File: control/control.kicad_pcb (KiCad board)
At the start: 2 copper layers, 100 x 40 mm, 54 parts, among them CON1 USB-MICRO-B, IC1 STM32F072CBT6, IC2 AD8495, IC3 ADP3335, P1 SWD, P2 CONN_02X04, P3 CONN_01X02, Q1 NPN, U1 ROTENC, U2 ESP8266, U3 ER-OLEDM023-1, U5 M3_HOLE, U6 M3_HOLE, U7 M3_HOLE, U8 M3_HOLE, X1 8MHz, X2 32k768

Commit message: first routing complete!
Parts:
- removed Q1: NPN, control:SOT23
- removed the R2 at (95.8, 127.8)
- added IC1: AD8542, control:MSOP8, B.Cu at (86.2, 136.5)
- added R1: 15k, control:R0603, B.Cu at (82.8, 135.5)
- added R3: 10k, control:R0603, B.Cu at (86.2, 129.5)
- added R5: 15k, control:R0603, B.Cu at (82.8, 133.5)
- added R6: 10k, control:R0603, B.Cu at (84.8, 129.5)
- moved SP1 13.2 mm to (98.5, 132.5), turned to 180 degrees
- moved BT1 12.4 mm to (110.5, 136.2), turned to 90 degrees
- moved C14 10.1 mm to (97.8, 113.2), turned to 0 degrees
- moved C15 9.40 mm to (97.8, 122.0), turned to 0 degrees
- moved C10 6.43 mm to (74.5, 107.8)
- moved C11 6.43 mm to (91.2, 109.5)
- moved C12 6.43 mm to (96.8, 109.5)
- moved C24 6.43 mm to (93.5, 122.2)
- moved C4 6.43 mm to (90.0, 111.2)
- moved C5 6.43 mm to (94.8, 121.0)
- moved C7 6.43 mm to (90.0, 112.5)
- moved C9 6.43 mm to (93.5, 121.0)
- moved IC2 6.43 mm to (91.0, 115.7)
- moved P1 6.43 mm to (81.0, 108.0)
- moved R7 6.43 mm to (96.0, 121.0)
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- renumbered C9 to C10, C12 to C11, C13 to C12, C19 to C13, C10 to C14, C11 to C15, C14 to C16, C15 to C17, C23 to C18, C24 to C19, C8 to C2, C25 to C20, C26 to C21, C16 to C22, C17 to C23, C18 to C24, C22 to C25, C2 to C3, C3 to C4, C4 to C5, C20 to C6, C5 to C7, C6 to C8, C7 to C9, IC1 to IC2, IC2 to IC4, R7 to R10, R9 to R11, R1 to R2, R3 to R4, R4 to R7, R5 to R8, R6 to R9, U3 to U4, X2 to X1, X1 to X2
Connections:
- IC2 pad 14: /PIEZO -> /PIEZO_A
- IC2 pad 15: /SYNC -> /PIEZO_B
- IC2 pad 18: /TRIAC -> /M_RELAY
- IC2 pad 20: /M_RELAY -> /TRIAC
- P2 pad 5: /SYNC -> Net-(P2-Pad5)
- P2 pad 7: VCC -> +5V
- P2 pad 8: +5V -> VCC
- SP1 pad 1: VCC -> Net-(IC1-Pad1)
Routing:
- net VDD: track 107.5 -> 283.8 mm, vias 0 -> 2
- net /ENC_BLU: track 0.00 -> 85.6 mm, vias 0 -> 4
- net /ENC_GRN: track 0.00 -> 81.8 mm, vias 0 -> 4
- net /ENC_SW: track 0.00 -> 81.4 mm, vias 0 -> 4
- net /ENC_B: track 3.42 -> 82.5 mm, vias 0 -> 4
- net /ENC_RED: track 0.00 -> 77.0 mm, vias 0 -> 4
- net /ENC_A: track 3.42 -> 75.7 mm, vias 0 -> 4
- net Net-(IC1-Pad2): track 0.00 -> 39.3 mm
- net /SYNC: track 30.0 -> 0.00 mm
- net Net-(BT1-Pad1): track 17.9 -> 42.8 mm
- net /nRST: track 1.55 -> 26.4 mm, vias 0 -> 5
- net VCC: track 51.3 -> 72.5 mm, vias 1 -> 0
- net Net-(IC1-Pad1): track 0.00 -> 19.1 mm
- net Net-(IC4-Pad5): track 69.4 -> 83.9 mm
- net /M_RELAY: track 30.2 -> 16.8 mm
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
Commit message: some routing improvements
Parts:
- added C26: 100n, control:C0603, B.Cu at (85.8, 129.5)
- moved R7 3.26 mm to (95.8, 117.8), turned to 180 degrees
- moved R3 0.75 mm to (87.0, 129.5)
- moved R6 0.25 mm to (84.5, 129.5)
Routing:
- net VDD: track 283.8 -> 292.8 mm
- net VCC: track 72.5 -> 75.7 mm
- net Net-(IC2-Pad6): track 5.91 -> 3.35 mm
- net Net-(C12-Pad2): track 10.7 -> 9.26 mm
- net Net-(C14-Pad1): track 11.0 -> 12.0 mm
- net Net-(C15-Pad1): track 5.65 -> 6.59 mm
- net Net-(IC1-Pad2): track 39.3 -> 38.6 mm
- net /PIEZO_A: track 7.32 -> 6.57 mm
- net GND: track 70.7 -> 71.1 mm, vias 18 -> 19

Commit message: update wifi, routing, gen gerbers, DONE r1
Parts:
- U2: value ESP8266 -> ESP8266-ESP01; footprint control:ESP8266 -> control:ESP8266-ESP01
- moved U2 19.1 mm to (55.7, 113.8), turned to 0 degrees
- moved C19 4.89 mm to (57.2, 130.1), turned to 180 degrees
- moved C8 1.25 mm to (81.5, 113.0)
- moved C3 1.20 mm to (81.5, 111.8)
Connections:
- CON1 pad 4: Net-(CON1-Pad4) -> (no net)
- CON1 pad 6: Net-(CON1-Pad6) -> (no net)
- CON1 pad 7: Net-(CON1-Pad7) -> (no net)
- IC2 pad 11: Net-(IC2-Pad11) -> (no net)
- IC2 pad 12: Net-(IC2-Pad12) -> (no net)
- IC2 pad 2: Net-(IC2-Pad2) -> (no net)
- IC2 pad 21: Net-(IC2-Pad21) -> (no net)
- IC2 pad 22: Net-(IC2-Pad22) -> /WIFI_RST
- IC2 pad 29: Net-(IC2-Pad29) -> /WIFI_GP0
- IC2 pad 40: Net-(IC2-Pad40) -> (no net)
- IC2 pad 45: Net-(IC2-Pad45) -> (no net)
- IC2 pad 46: Net-(IC2-Pad46) -> (no net)
- IC4 pad 4: Net-(IC4-Pad4) -> (no net)
- P1 pad 6: Net-(P1-Pad6) -> (no net)
- P1 pad 7: Net-(P1-Pad7) -> (no net)
- P1 pad 8: Net-(P1-Pad8) -> (no net)
- P2 pad 5: Net-(P2-Pad5) -> (no net)
- U2 pad 1: /WIFI_TX -> /WIFI_RX
- U2 pad 2: GND -> /WIFI_GP0
- U2 pad 3: Net-(U2-Pad3) -> (no net)
- U2 pad 4: Net-(U2-Pad4) -> GND
- U2 pad 5: Net-(U2-Pad5) -> /WIFI_TX
- U2 pad 6: Net-(U2-Pad6) -> VDD
- U2 pad 7: VDD -> /WIFI_RST
- U2 pad 8: /WIFI_RX -> VDD
- U4 pad 17: Net-(U4-Pad17) -> (no net)
- U4 pad 18: Net-(U4-Pad18) -> (no net)
- U4 pad 19: Net-(U4-Pad19) -> (no net)
- U4 pad 3: Net-(U4-Pad3) -> (no net)
- U4 pad 9: Net-(U4-Pad9) -> (no net)
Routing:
- net /WIFI_GP0: track 0.00 -> 18.9 mm, vias 0 -> 1
- net VDD: track 292.8 -> 307.3 mm
- net /WIFI_RST: track 0.00 -> 7.45 mm, vias 0 -> 1
- net VCC: track 75.7 -> 72.0 mm
- net /WIFI_RX: track 15.8 -> 13.6 mm
- net +5V: track 47.2 -> 45.1 mm
- net /WIFI_TX: track 5.82 -> 4.33 mm
- net /USB_DP: track 30.2 -> 30.9 mm
- net /USB_DM: track 30.1 -> 30.8 mm
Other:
- board text added: "ADAM GREIG DAVID TURNER JON SOWMAN"
- board text added: "GRN"
- board text added: "SUPERVIDE CONTROL BOARD"
- board text added: "r1 2014-03-06"
- board text added: "r1 2015-03-06"

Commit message: fix a few derps, actually DONE r1
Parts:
- moved C13 1.77 mm to (69.2, 105.0), turned to 180 degrees
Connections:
- U4 pad 1: VDD -> GND
- U4 pad 2: GND -> VDD
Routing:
- net VDD: track 307.3 -> 315.9 mm

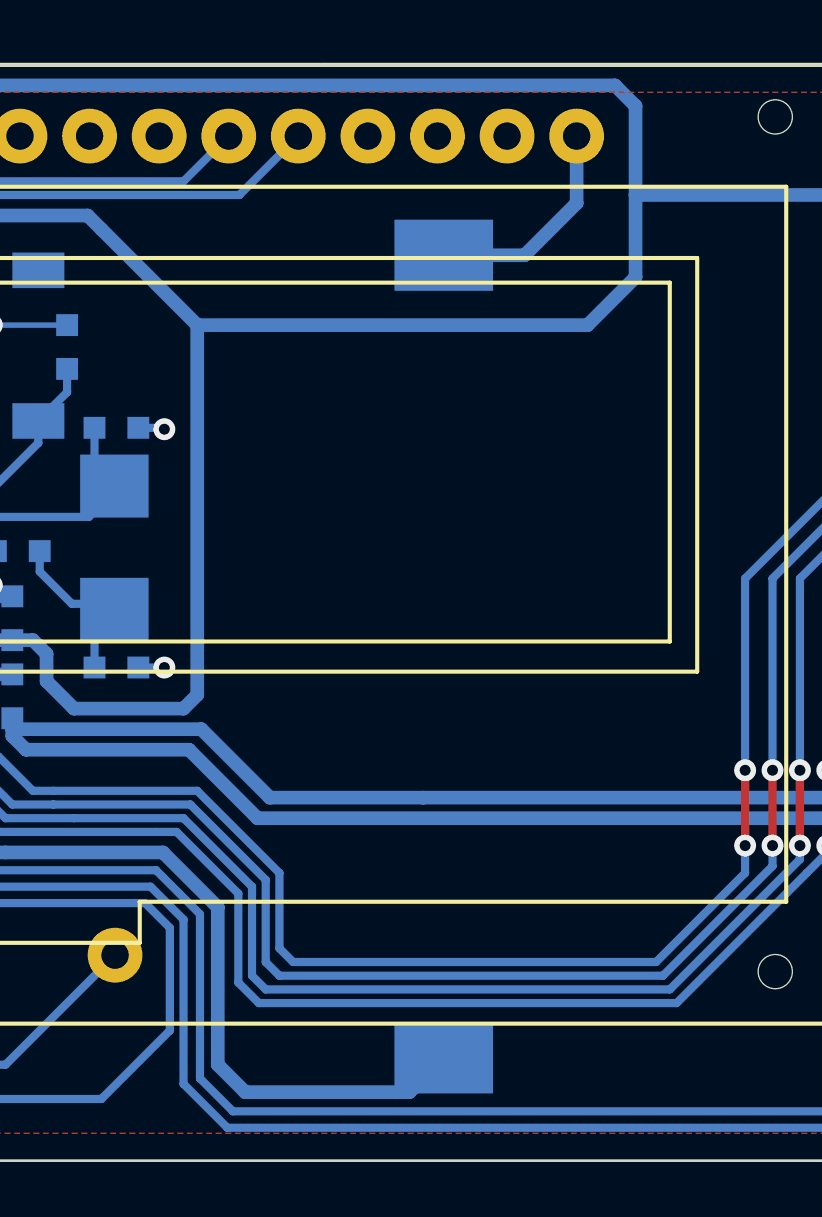
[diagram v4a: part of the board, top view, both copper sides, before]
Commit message: shift coin cell a little to make more space. still r1.
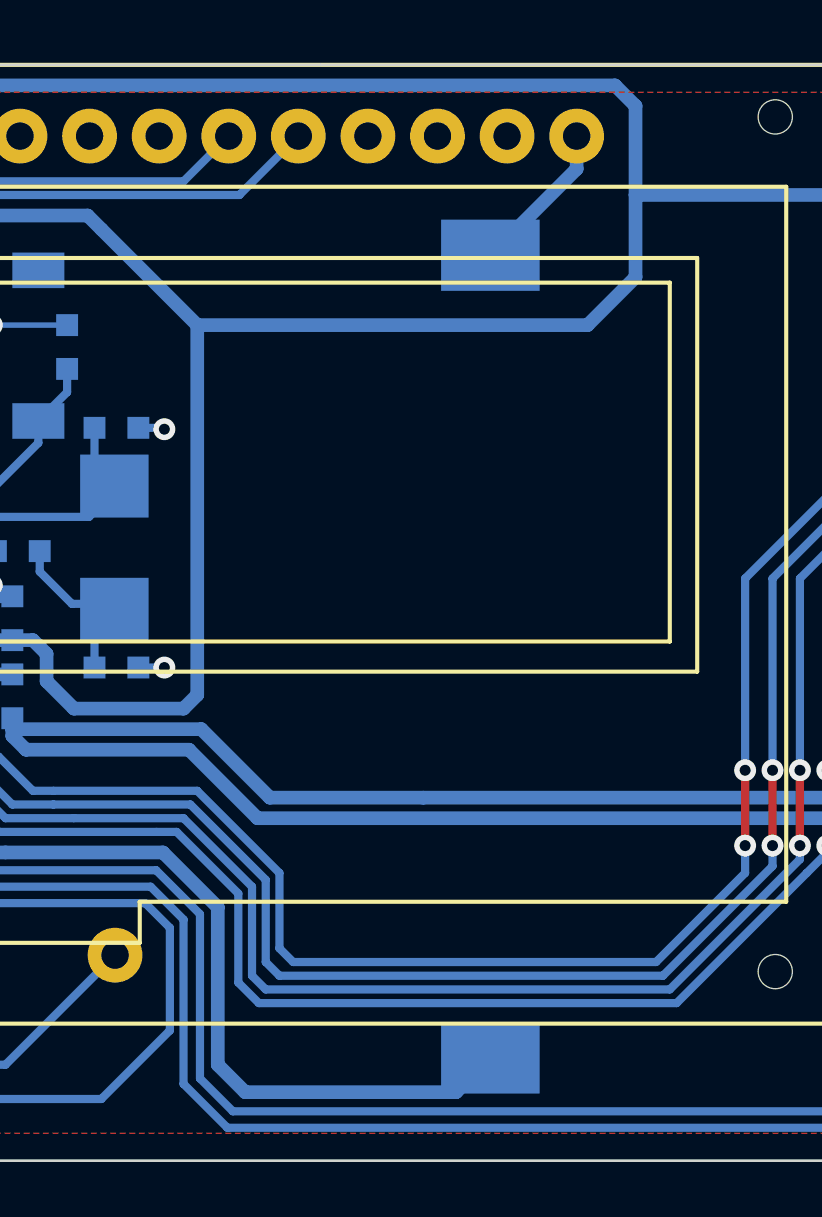
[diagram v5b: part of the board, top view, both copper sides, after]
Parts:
- moved BT1 1.70 mm to (112.2, 136.2)
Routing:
- net GND: track 71.1 -> 68.7 mm
- net Net-(BT1-Pad1): track 42.8 -> 44.5 mm

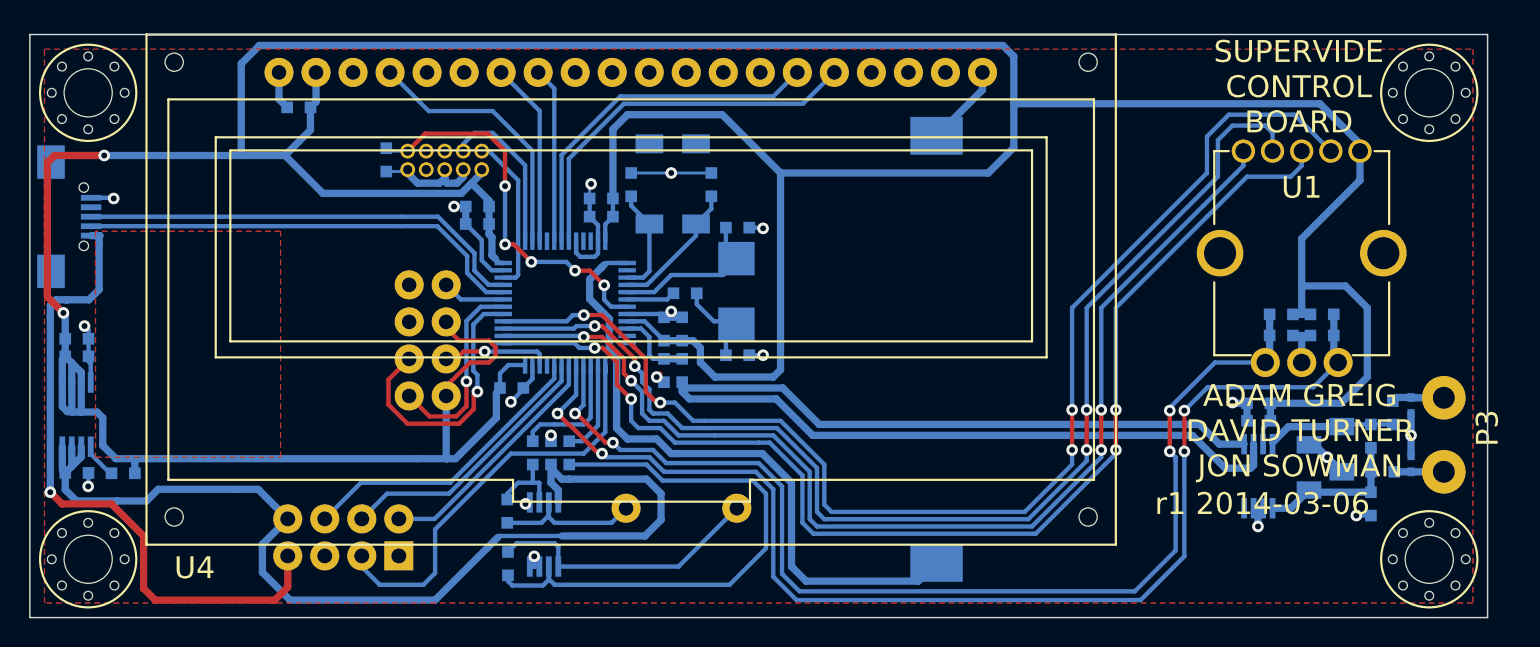
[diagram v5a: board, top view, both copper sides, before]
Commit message: regen gerbils w/ correct date on silk
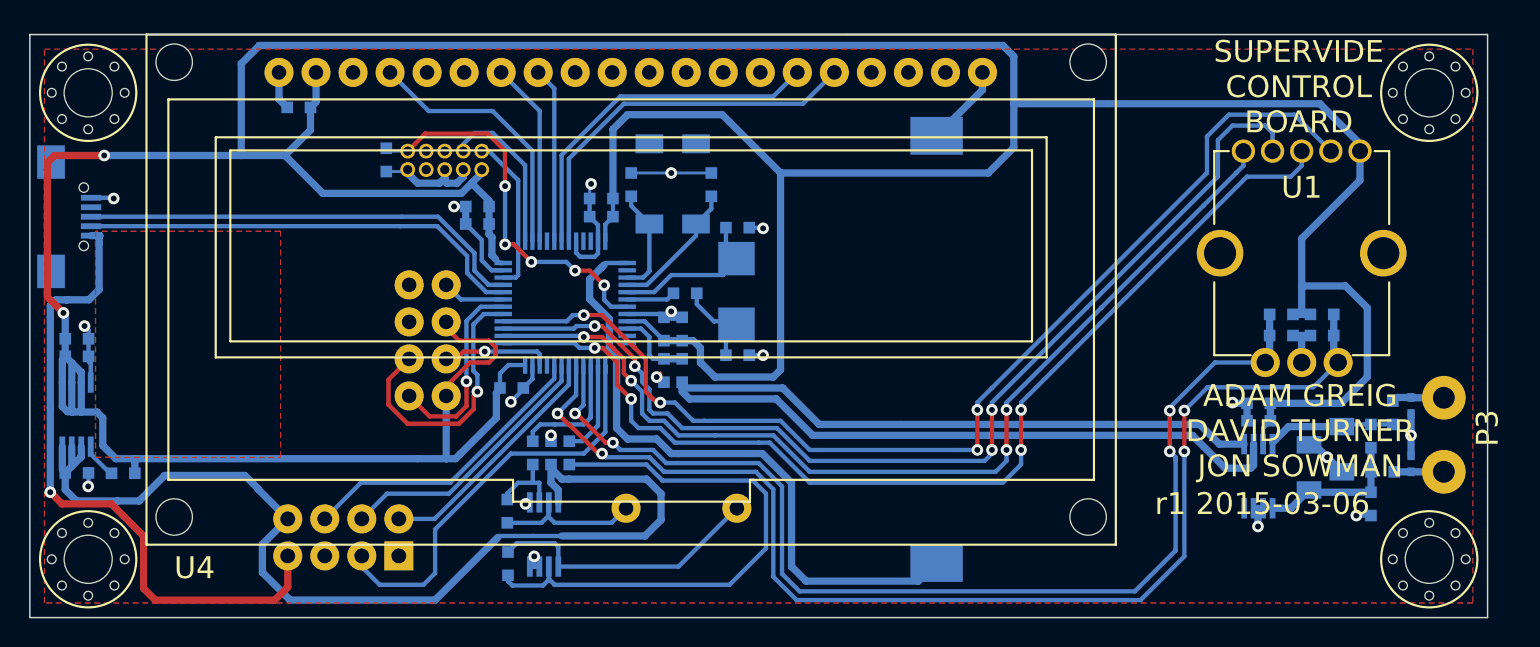
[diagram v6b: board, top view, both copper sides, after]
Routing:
- net /ENC_BLU: track 85.6 -> 76.0 mm
- net /ENC_GRN: track 81.8 -> 72.6 mm
- net /ENC_RED: track 76.8 -> 68.1 mm
- net /ENC_SW: track 81.4 -> 73.3 mm
- net VCC: track 72.0 -> 72.8 mm
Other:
- board text removed: "r1 2014-03-06"

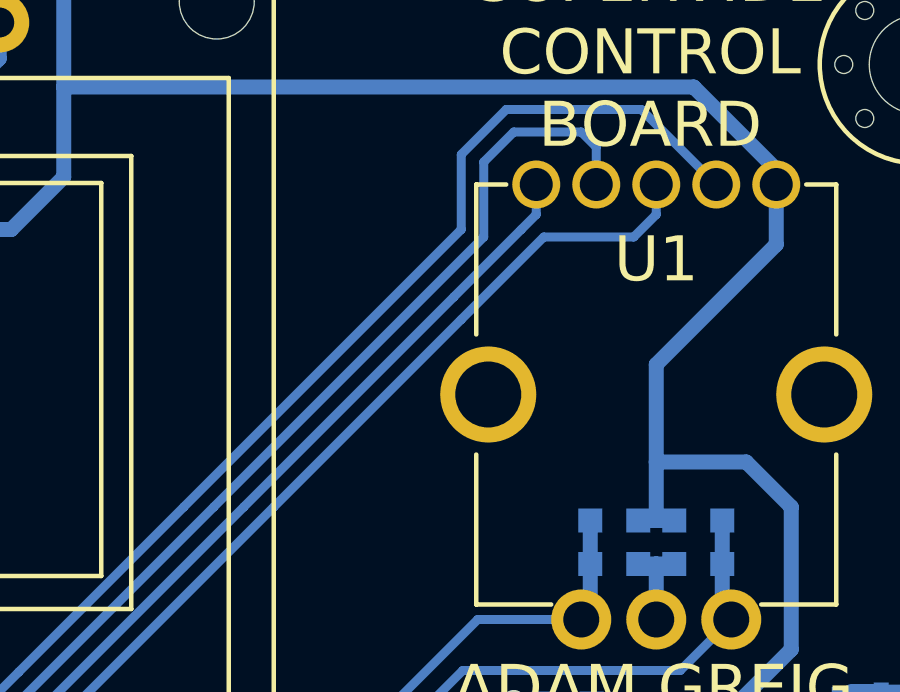
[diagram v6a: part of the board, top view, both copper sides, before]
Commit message: add resistor to red LED, closes #4
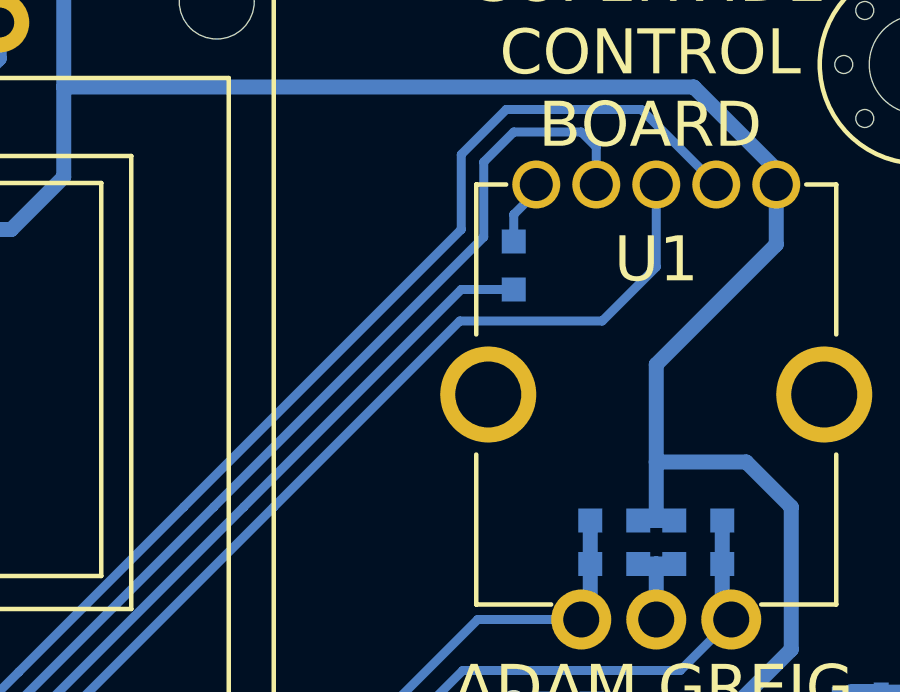
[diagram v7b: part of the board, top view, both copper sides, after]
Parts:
- added R12: 50R, control:R0603, B.Cu at (132.5, 111.5)
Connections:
- U1 pad 1: /ENC_RED -> Net-(R12-Pad2)
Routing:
- net /ENC_RED: track 68.1 -> 65.4 mm
- net Net-(R12-Pad2): track 0.00 -> 2.21 mm
- net /ENC_SW: track 73.3 -> 74.3 mm

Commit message: add strain relief for tc, closes #5
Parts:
- added REF**: HOLE, control:HOLE, F.Cu at (147.0, 119.0)
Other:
- board text added: "r2 2015-10-04"
- board text removed: "r1 2015-03-06"
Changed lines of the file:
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@@
     (tracks 697)
     (zones 0)
-    (modules 59)
+    (modules 60)
     (nets 49)
   )
@@
       (net 48 "Net-(R12-Pad2)"))
   )
-  (gr_text "r1 2015-03-06" (at 132.5 137) (layer B.SilkS)
+  (module control:HOLE (layer F.Cu)
+    (at 147 119)
+    (fp_text reference REF** (at 0 0.5) (layer F.SilkS) hide
+      (effects (font (size 1 1) (thickness 0.15)))
+    )
+    (fp_text value HOLE (at 0 -0.5) (layer F.Fab) hide
+      (effects (font (size 1 1) (thickness 0.15)))
+    )
+    (pad "" np_thru_hole circle (at 0 0) (size 3 3) (drill 3) (layers *.Cu *.Mask F.SilkS))
+  )
+  (gr_text "r2 2015-10-04" (at 132.5 137) (layer B.SilkS)
     (effects (font (size 1.5 1.5) (thickness 0.3)) (justify mirror))
   )
@@
   (gr_line (start 105.5 134.5) (end 107.5 134.5) (angle 90) (layer B.SilkS) (width 0.2))
   (gr_line (start 106.5 133.5) (end 106.5 135.5) (angle 90) (layer B.SilkS) (width 0.2))
-  (gr_text "r1 2015-03-06" (at 134.55 132.2) (layer F.SilkS)
+  (gr_text "r2 2015-10-04" (at 134.55 132.2) (layer F.SilkS)
     (effects (font (size 1.5 1.5) (thickness 0.3)))
   )
